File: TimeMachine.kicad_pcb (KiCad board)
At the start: 4 copper layers, 107.6 x 59.8 mm, 53 parts, among them J1 AppleIIBus, J2 JTAG, U1 EPM7128SL84, U2 DS1215, U3 74AHCT04, U4 AS6C8008, U5 39F040, Y1 32k768

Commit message: Can't fit...
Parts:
- removed C22, C23: 6p, stdpads:C_0805
- Y1: footprint stdpads:Crystal_HC49-SMD -> Crystal_C26-LF_D2.1mm_L6.5mm_Horizontal_1EP_style1
- moved Y1 0.90 mm to (146.1, 115.6), turned to 0 degrees
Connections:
- U1 pad 15: /~INH~ -> /RA18
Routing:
- net /RA18: track 11.6 -> 64.3 mm, vias 0 -> 5
- net /~INH~: track 30.4 -> 0.00 mm, vias 1 -> 0
- net Net-(U2-Pad2): track 12.5 -> 3.36 mm
- net GND: track 157.1 -> 152.2 mm, vias 487 -> 479
- net Net-(U2-Pad1): track 9.87 -> 5.78 mm

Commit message: Lots of state machine work
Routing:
- net /RA18: track 64.3 -> 76.5 mm
- net GND: vias 479 -> 493
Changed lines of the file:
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@@
     (thickness 1.6)
     (drawings 30)
-    (tracks 1908)
+    (tracks 1922)
     (zones 0)
     (modules 51)
@@
   (via (at 204.724 99.06) (size 0.6) (drill 0.3) (layers F.Cu B.Cu) (net 2))
   (via (at 204.343 103.124) (size 0.6) (drill 0.3) (layers F.Cu B.Cu) (net 2))
-  (via (at 219.837 106.045) (size 0.6) (drill 0.3) (layers F.Cu B.Cu) (net 2))
+  (via (at 220.091 106.045) (size 0.6) (drill 0.3) (layers F.Cu B.Cu) (net 2))
   (via (at 215.9 106.934) (size 0.6) (drill 0.3) (layers F.Cu B.Cu) (net 2))
   (via (at 224.917 106.934) (size 0.6) (drill 0.3) (layers F.Cu B.Cu) (net 2))
@@
   (via (at 205.359 114.681) (size 0.6) (drill 0.3) (layers F.Cu B.Cu) (net 2))
   (via (at 214.757 115.951) (size 0.6) (drill 0.3) (layers F.Cu B.Cu) (net 2))
-  (via (at 223.774 109.601) (size 0.6) (drill 0.3) (layers F.Cu B.Cu) (net 2))
+  (via (at 223.52 109.601) (size 0.6) (drill 0.3) (layers F.Cu B.Cu) (net 2))
   (via (at 225.425 102.235) (size 0.6) (drill 0.3) (layers F.Cu B.Cu) (net 2))
   (via (at 219.837 102.362) (size 0.6) (drill 0.3) (layers F.Cu B.Cu) (net 2))
   (via (at 219.837 98.425) (size 0.6) (drill 0.3) (layers F.Cu B.Cu) (net 2))
-  (via (at 216.408 102.362) (size 0.6) (drill 0.3) (layers F.Cu B.Cu) (net 2))
-  (via (at 216.408 99.695) (size 0.6) (drill 0.3) (layers F.Cu B.Cu) (net 2))
+  (via (at 215.9 102.362) (size 0.6) (drill 0.3) (layers F.Cu B.Cu) (net 2))
+  (via (at 219.837 99.695) (size 0.6) (drill 0.3) (layers F.Cu B.Cu) (net 2))
   (via (at 216.408 97.155) (size 0.6) (drill 0.3) (layers F.Cu B.Cu) (net 2))
   (via (at 205.105 100.584) (size 0.6) (drill 0.3) (layers F.Cu B.Cu) (net 2))
@@
   (via (at 183.007 96.012) (size 0.6) (drill 0.3) (layers F.Cu B.Cu) (net 2))
   (via (at 180.721 96.012) (size 0.6) (drill 0.3) (layers F.Cu B.Cu) (net 2))
-  (via (at 210.439 98.425) (size 0.6) (drill 0.3) (layers F.Cu B.Cu) (net 2))
+  (via (at 207.01 98.425) (size 0.6) (drill 0.3) (layers F.Cu B.Cu) (net 2))
   (via (at 210.185 106.934) (size 0.6) (drill 0.3) (layers F.Cu B.Cu) (net 2))
   (via (at 218.059 109.601) (size 0.6) (drill 0.3) (layers F.Cu B.Cu) (net 2))
@@
   (segment (start 151.306 119.38) (end 149.225 119.38) (width 0.508) (layer F.Cu) (net 2))
   (via (at 149.225 119.38) (size 0.8) (drill 0.4) (layers F.Cu B.Cu) (net 2))
+  (via (at 209.55 102.235) (size 0.6) (drill 0.3) (layers F.Cu B.Cu) (net 2))
+  (via (at 209.55 100.965) (size 0.6) (drill 0.3) (layers F.Cu B.Cu) (net 2))
+  (via (at 208.28 99.695) (size 0.6) (drill 0.3) (layers F.Cu B.Cu) (net 2))
+  (via (at 213.36 99.695) (size 0.6) (drill 0.3) (layers F.Cu B.Cu) (net 2))
+  (via (at 211.455 97.155) (size 0.6) (drill 0.3) (layers F.Cu B.Cu) (net 2))
+  (via (at 212.09 98.425) (size 0.6) (drill 0.3) (layers F.Cu B.Cu) (net 2))
+  (via (at 214.63 100.965) (size 0.6) (drill 0.3) (layers F.Cu B.Cu) (net 2))
+  (via (at 219.837 100.965) (size 0.6) (drill 0.3) (layers F.Cu B.Cu) (net 2))
+  (via (at 216.408 98.425) (size 0.6) (drill 0.3) (layers F.Cu B.Cu) (net 2))
+  (via (at 216.408 99.695) (size 0.6) (drill 0.3) (layers F.Cu B.Cu) (net 2))
+  (via (at 216.408 100.965) (size 0.6) (drill 0.3) (layers F.Cu B.Cu) (net 2))
+  (via (at 219.964 97.155) (size 0.6) (drill 0.3) (layers F.Cu B.Cu) (net 2))
+  (via (at 221.615 106.934) (size 0.6) (drill 0.3) (layers F.Cu B.Cu) (net 2))
+  (via (at 221.742 109.601) (size 0.6) (drill 0.3) (layers F.Cu B.Cu) (net 2))
   (via (at 174.625 113.03) (size 0.6) (drill 0.3) (layers F.Cu B.Cu) (net 3))
   (segment (start 174.625 113.03) (end 176.0475 113.03) (width 0.1524) (layer F.Cu) (net 3))
@@
   (segment (start 223.52 124.46) (end 227.203 128.143) (width 0.1524) (layer B.Cu) (net 37))
   (segment (start 227.203 128.397) (end 226.06 129.54) (width 0.1524) (layer B.Cu) (net 37))
-  (via (at 226.06 113.03) (size 0.6) (drill 0.3) (layers F.Cu B.Cu) (net 78))
-  (segment (start 227.71 113.03) (end 226.06 113.03) (width 0.1524) (layer F.Cu) (net 78))
-  (segment (start 220.472 107.442) (end 226.06 113.03) (width 0.1524) (layer B.Cu) (net 78))
-  (segment (start 220.472 102.108) (end 220.472 107.442) (width 0.1524) (layer B.Cu) (net 78))
-  (segment (start 220.98 101.6) (end 220.472 102.108) (width 0.1524) (layer B.Cu) (net 78))
-  (via (at 220.98 101.6) (size 0.6) (drill 0.3) (layers F.Cu B.Cu) (net 78))
   (via (at 212.09 130.175) (size 0.6) (drill 0.3) (layers F.Cu B.Cu) (net 40))
   (segment (start 212.09 129.22) (end 212.09 130.175) (width 0.1524) (layer F.Cu) (net 40))
@@
   (segment (start 185.42 106.22) (end 185.42 107.4625) (width 0.1524) (layer F.Cu) (net 77))
   (segment (start 185.2 106) (end 185.42 106.22) (width 0.1524) (layer F.Cu) (net 77))
+  (via (at 226.06 113.03) (size 0.6) (drill 0.3) (layers F.Cu B.Cu) (net 78))
+  (segment (start 227.71 113.03) (end 226.06 113.03) (width 0.1524) (layer F.Cu) (net 78))
+  (via (at 220.98 101.6) (size 0.6) (drill 0.3) (layers F.Cu B.Cu) (net 78))
   (segment (start 179.705 104.14) (end 181.61 106.045) (width 0.1524) (layer F.Cu) (net 78))
   (segment (start 181.61 106.045) (end 181.61 107.4625) (width 0.1524) (layer F.Cu) (net 78))
@@
   (segment (start 182.245 108.585) (end 187.96 108.585) (width 0.1524) (layer B.Cu) (net 78))
   (segment (start 181.61 109.22) (end 182.245 108.585) (width 0.1524) (layer B.Cu) (net 78))
+  (segment (start 220.98 101.6) (end 208.28 101.6) (width 0.1524) (layer F.Cu) (net 78))
+  (segment (start 220.98 107.95) (end 226.06 113.03) (width 0.1524) (layer B.Cu) (net 78))
+  (segment (start 220.98 101.6) (end 220.98 107.95) (width 0.1524) (layer B.Cu) (net 78))
   (segment (start 199.01 105.41) (end 194.564 105.41) (width 0.1524) (layer F.Cu) (net 79))
   (segment (start 194.564 105.41) (end 193.294 104.14) (width 0.1524) (layer F.Cu) (net 79))

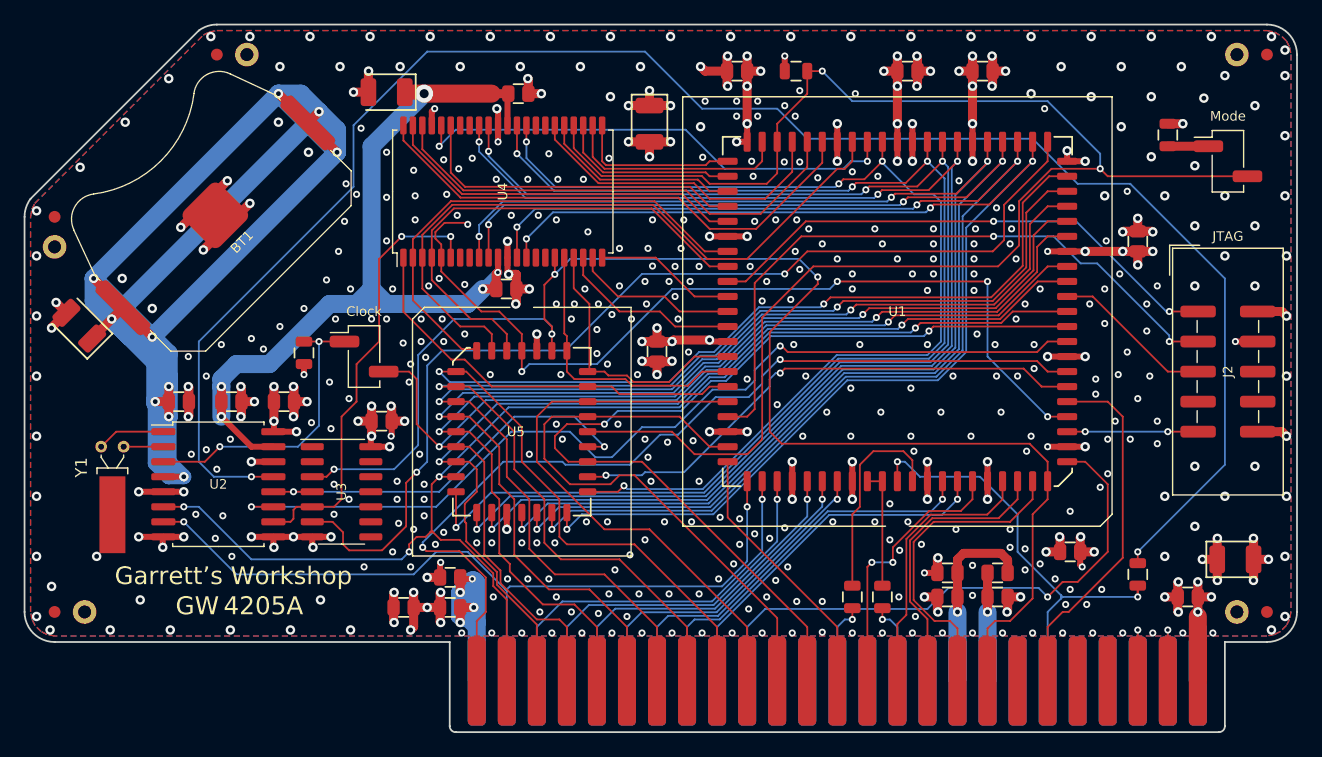
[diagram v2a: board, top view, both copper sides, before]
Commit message: Merged changes from GR8RAM, e.g. pipelined add
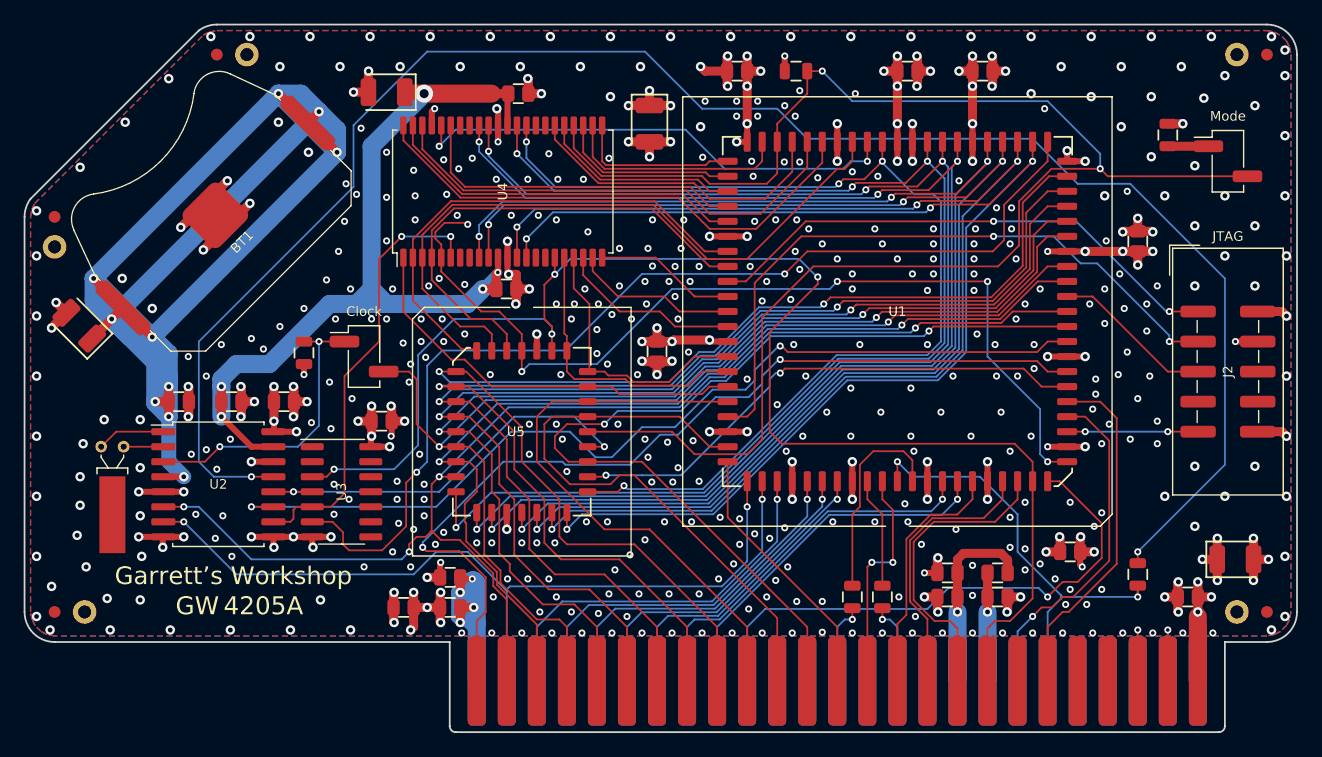
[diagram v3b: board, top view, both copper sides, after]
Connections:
- U1 pad 10: /A15 -> /R~W~
- U1 pad 11: /R~W~ -> /~DEVSEL~
- U1 pad 12: /~DEVSEL~ -> /RA18
- U1 pad 15: /RA18 -> /~INH~
- U1 pad 6: /A12 -> /A13
- U1 pad 8: /A13 -> /A14
- U1 pad 84: /7Mr -> /A12
- U1 pad 9: /A14 -> /A15
- Y1 pad 3: (no net) -> GND
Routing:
- net /~INH~: track 0.00 -> 29.0 mm, vias 0 -> 1
- net +BATT: track 166.7 -> 153.5 mm
- net /A12: track 23.2 -> 19.2 mm
- net /RA18: track 76.5 -> 80.3 mm
- net /A13: track 23.4 -> 20.8 mm
- net /R~W~: track 123.9 -> 122.1 mm
- net /~DEVSEL~: track 48.2 -> 46.6 mm
- net /A14: track 24.6 -> 23.3 mm
- net /A15: track 27.1 -> 25.9 mm
- net /~IOSTRB~: track 30.5 -> 29.7 mm
- net /7Mr: track 10.1 -> 9.36 mm
- net GND: vias 493 -> 508

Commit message: Fixed mistake, submitted to JLCPCB
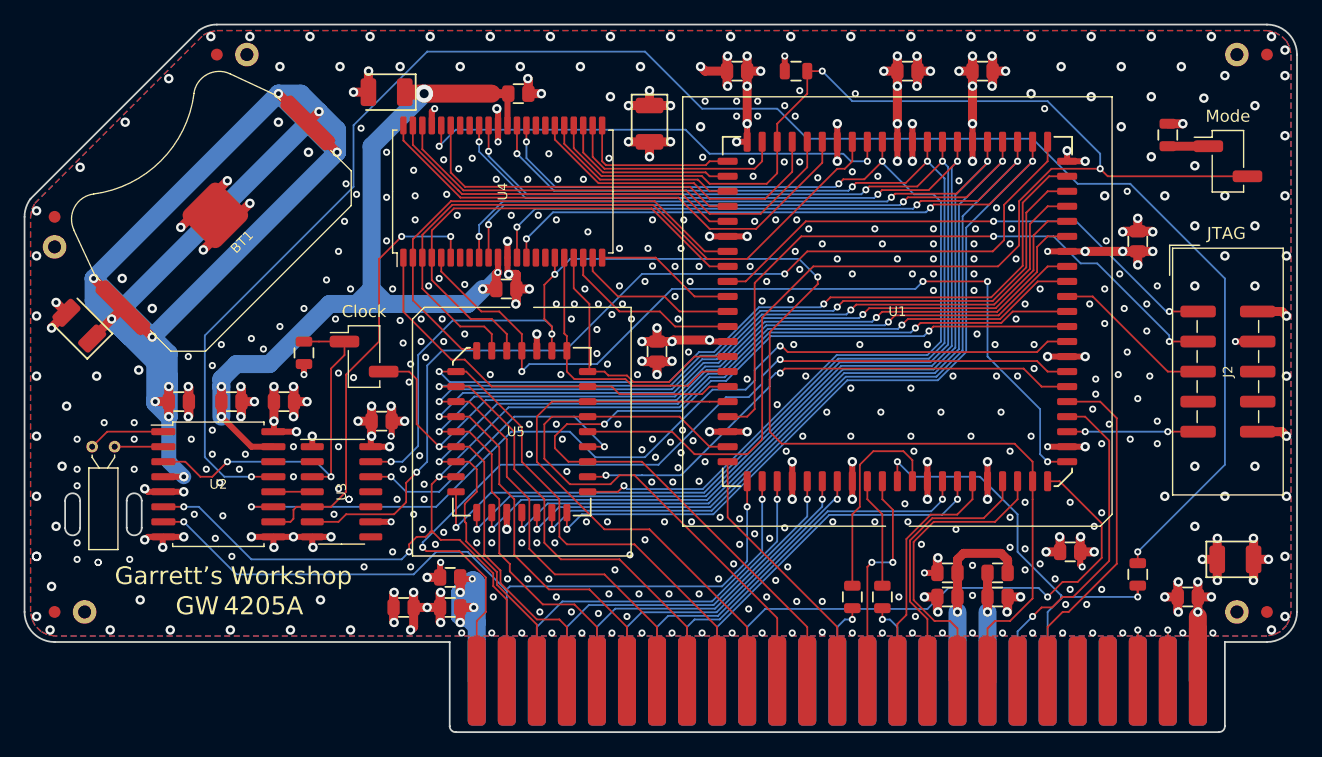
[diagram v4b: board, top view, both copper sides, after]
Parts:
- R3: value 100 -> 15
- Y1: footprint Crystal_C26-LF_D2.1mm_L6.5mm_Horizontal_1EP_style1 -> Crystal:Crystal_C26-LF_D2.1mm_L6.5mm_Horizontal
- moved Y1 0.76 mm to (145.3, 115.6)
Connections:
- JP2 pad 1: /CA2 -> /DS~WE~
- R4 pad 1: /CA2 -> /DS~WE~
- U2 pad 12: /~OE~ -> /DS~OE~
- U2 pad 3: /CA2 -> /DS~WE~
- U3 pad 12: Net-(U3-Pad12) -> /~OE~
- U3 pad 13: GND -> /R~W~
- U3 pad 3: /R~W~ -> /DS~WE~
- U3 pad 4: /~OE~ -> /DS~OE~
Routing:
- net /DS~WE~: track 0.00 -> 32.7 mm, vias 0 -> 2
- net /CA2: track 25.0 -> 0.00 mm, vias 2 -> 0
- net /~OE~: track 34.7 -> 25.4 mm
- net /R~W~: track 122.1 -> 116.6 mm
- net /RA18: track 80.3 -> 74.9 mm, vias 5 -> 4
- net /RAMROMCSgb: track 87.7 -> 83.9 mm
- net /DS~OE~: track 0.00 -> 3.29 mm
- net /C~RES~: track 152.0 -> 151.1 mm
- net Net-(U2-Pad2): track 3.36 -> 4.12 mm
- net Net-(U2-Pad1): track 5.78 -> 6.54 mm
- net /RAMCS: track 41.9 -> 41.4 mm
- net GND: vias 508 -> 521
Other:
- outline, holes or cut-outs redrawn
